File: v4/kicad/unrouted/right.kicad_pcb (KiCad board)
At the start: 2 copper layers, 160 x 118.6 mm, 72 parts

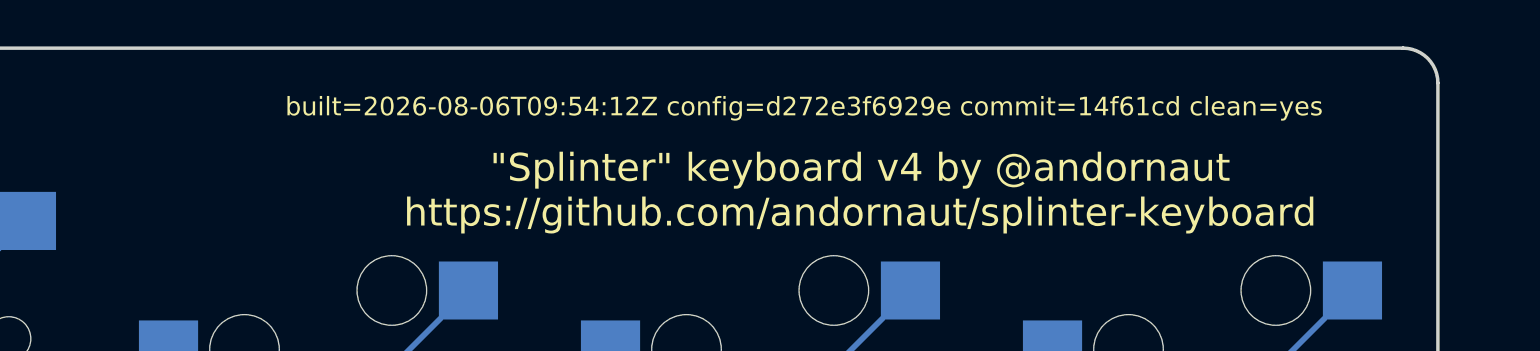
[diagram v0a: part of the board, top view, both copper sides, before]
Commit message: Rebuild the v4 boards from config d272e3f6929e
Pipeline re-run with no config change: new provenance stamp, reordered
items and re-tessellated zone fills. Tracks, vias and footprints are
unchanged on all four boards. KiCad 10 adds td_enabled and empty net
color/assignment maps to each .kicad_pro.
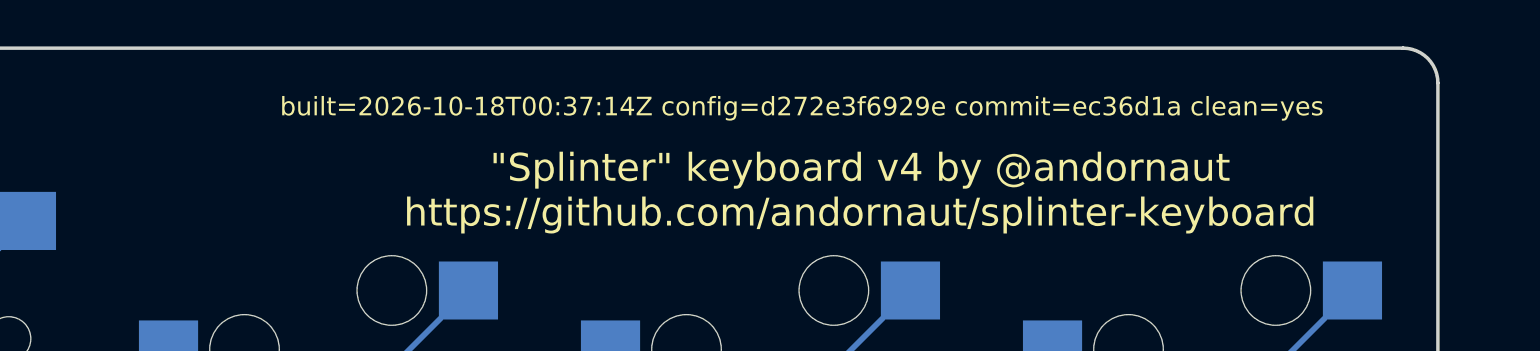
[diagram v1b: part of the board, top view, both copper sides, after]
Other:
- board text added: "built=2026-10-18T00:37:14Z config=d272e3f6929e commit=ec36d1a clean=yes"
- board text removed: "built=2026-08-06T09:54:12Z config=d272e3f6929e commit=14f61cd clean=yes"

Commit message: Wire the v4 TRRS jack per contact and drop the data resistor
- Remove the 100R series resistor from the split data line. QMK's RP2040
  half-duplex driver has the receiving half drive the line high while the
  sender pulls it low, so series resistance lifts the low past the input
  threshold and the link fails.
- Add trrs_hc_pj320a, a single-sided HC-PJ-320A-4P-D footprint with one pad
  per contact at HCTL's recommended positions. Wire tip VCC, ring 2 GP2,
  sleeve GND and leave ring 1 open.
- Re-route the jack and TVS on both halves with the TVS in line.
- Check the jack's contact nets in validate:firmware, and treat the jack as
  non-mirrorable in validate:symmetry.
- Remove the plate wall down to the plate over the TRRS corner, with a 29.00
  relief, so no case surface can touch the jack's exposed contacts. Update
  gen-case.py, BUILD.md and the Onshape exports.
- Document the split connection, the 3.6V Liatris VCC jumper and the
  no-hot-plug rule.
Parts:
- removed R1: 100R, splinter:R_0805
- TRRS1: footprint ceoloide:trrs_pj320a (reversible, symmetric) -> splinter:trrs_hc_pj320a
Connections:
- D33 pad A: DATA_RAW -> P2
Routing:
- net DATA_RAW: track 31.4 -> 0.00 mm
- net P2: track 19.5 -> 37.4 mm
- net GND: track 81.0 -> 71.2 mm
- net P16: track 178.1 -> 169.7 mm
- net P15: track 147.6 -> 139.2 mm
- net P14: track 198.9 -> 190.5 mm
- net P10: track 150.6 -> 142.2 mm
- net P9: track 199.0 -> 194.2 mm
- net dash_upper: track 13.7 -> 12.5 mm, vias 1 -> 0
- net dash_num: track 13.7 -> 12.5 mm, vias 1 -> 0
- net dash_lower: track 13.7 -> 12.5 mm, vias 1 -> 0
- net dash_home: track 13.7 -> 12.5 mm, vias 1 -> 0
- net zero_upper: track 13.7 -> 12.5 mm, vias 1 -> 0
- net zero_num: track 13.7 -> 12.5 mm, vias 1 -> 0
- net zero_lower: track 13.7 -> 12.5 mm, vias 1 -> 0
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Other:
- board text added: "built=2026-10-18T19:11:44Z config=fba23081ee07 commit=0d913c5 clean=no"
- board text removed: "Resistor 100R 1% UNI-ROYAL 0805W8F- 1000T5E 0805"
- board text removed: "built=2026-10-18T00:37:14Z config=d272e3f6929e commit=ec36d1a clean=yes"

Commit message: Rebuild the v4 boards from config fba23081ee07
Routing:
- net P15: track 139.2 -> 147.6 mm
- net P14: track 190.5 -> 198.9 mm
- net P16: track 169.7 -> 178.1 mm
- net P10: track 142.2 -> 150.6 mm
- net P9: track 194.2 -> 199.0 mm
- net dash_upper: track 12.5 -> 13.7 mm, vias 0 -> 1
- net dash_num: track 12.5 -> 13.7 mm, vias 0 -> 1
- net dash_lower: track 12.5 -> 13.7 mm, vias 0 -> 1
- net dash_home: track 12.5 -> 13.7 mm, vias 0 -> 1
- net zero_upper: track 12.5 -> 13.7 mm, vias 0 -> 1
- net zero_num: track 12.5 -> 13.7 mm, vias 0 -> 1
- net zero_lower: track 12.5 -> 13.7 mm, vias 0 -> 1
- net zero_home: track 12.5 -> 13.7 mm, vias 0 -> 1
- net mirror_three_mod: track 13.3 -> 14.5 mm, vias 0 -> 1
- net mirror_four_upper: track 12.5 -> 13.7 mm, vias 0 -> 1
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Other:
- board text added: "built=2026-10-18T19:58:37Z config=fba23081ee07 commit=c602086 clean=yes"
- board text removed: "built=2026-10-18T19:11:44Z config=fba23081ee07 commit=0d913c5 clean=no"

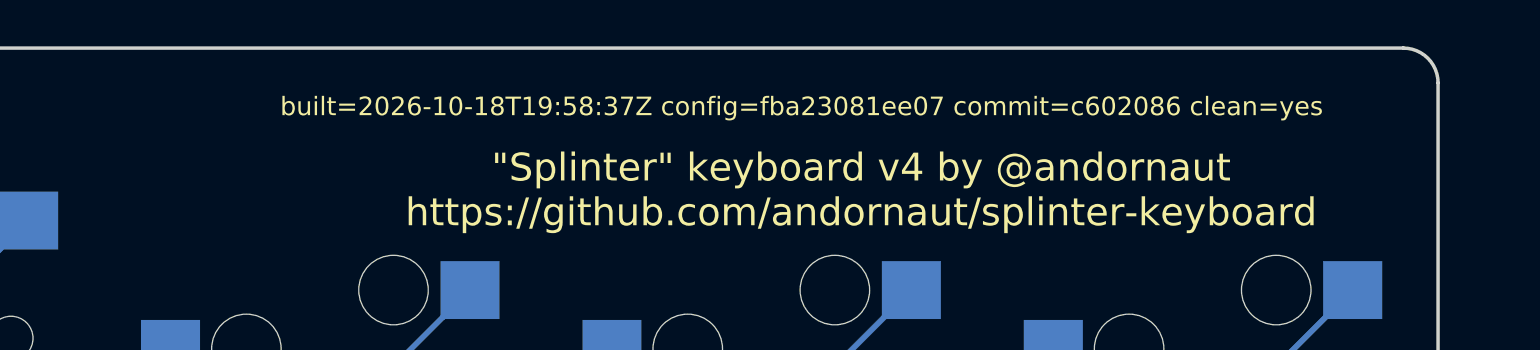
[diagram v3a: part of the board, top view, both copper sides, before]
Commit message: Have JLCPCB place the v4 reset switch
- Add sw_skqgabe010, a fork of ergogen's button footprint whose module layer
  follows `side`, so the position file reports the back-side reset switch on
  the Bottom instead of the bare Top. Pads and silk are unchanged.
- Assign C115351 (ALPS SKQGABE010) in jlcpcb-parts.json at rotation 0: the
  footprint matches JLCPCB's KEY-SMD_4P-L5.2-W5.2-P3.70-LS6.4 at 0 degrees.
- Move the reset switch from hand-soldered to placed by JLCPCB in the v4
  fabrication docs.
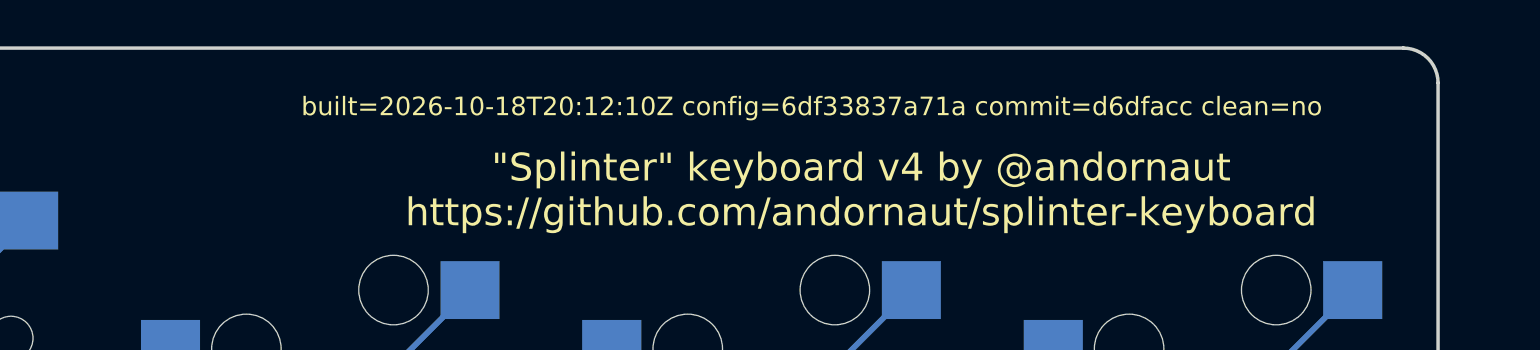
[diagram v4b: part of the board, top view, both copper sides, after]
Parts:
- B1: moved to B.Cu
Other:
- board text added: "built=2026-10-18T20:12:10Z config=6df33837a71a commit=d6dfacc clean=no"
- board text removed: "built=2026-10-18T19:58:37Z config=fba23081ee07 commit=c602086 clean=yes"

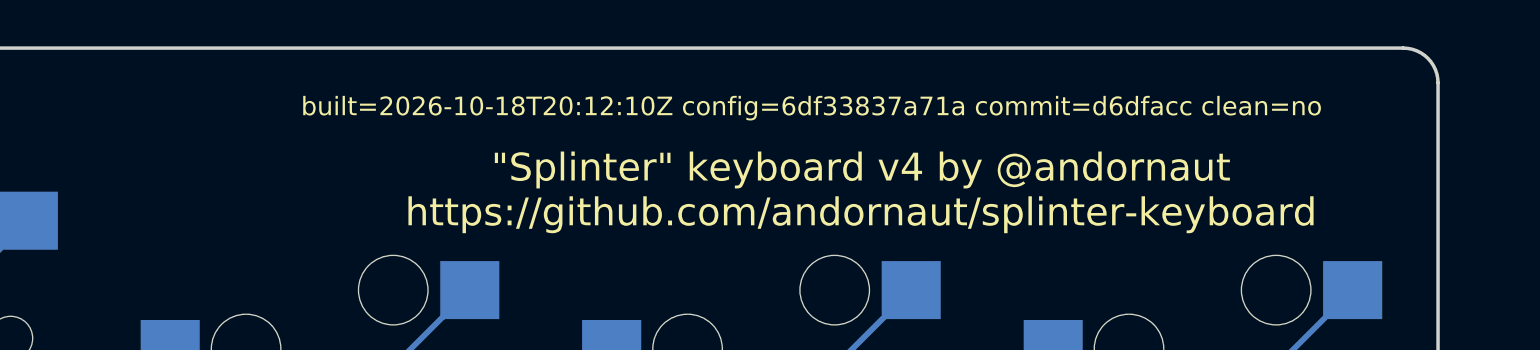
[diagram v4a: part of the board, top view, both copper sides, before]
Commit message: Rebuild the v4 boards from config 6df33837a71a
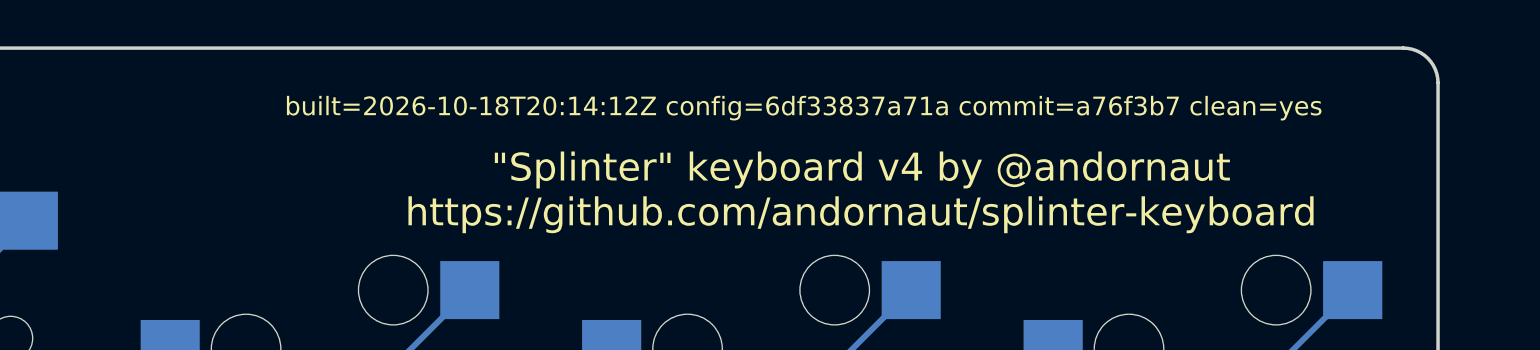
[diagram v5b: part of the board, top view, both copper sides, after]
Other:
- board text added: "built=2026-10-18T20:14:12Z config=6df33837a71a commit=a76f3b7 clean=yes"
- board text removed: "built=2026-10-18T20:12:10Z config=6df33837a71a commit=d6dfacc clean=no"

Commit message: Keep copper out from under the v4 reset switch frame
Add a back-copper rule area between each side's two reset-switch pads, the
prohibited area for copper tracks on ALPS's SKQG land drawing. It disallows
pour, tracks and vias on the switch's own layer only, so the F.Cu matrix
traces under the switch stay. add-keepout-zones.py maps the area from the
footprint frame through the switch's own pads, so it follows the part on both
halves.
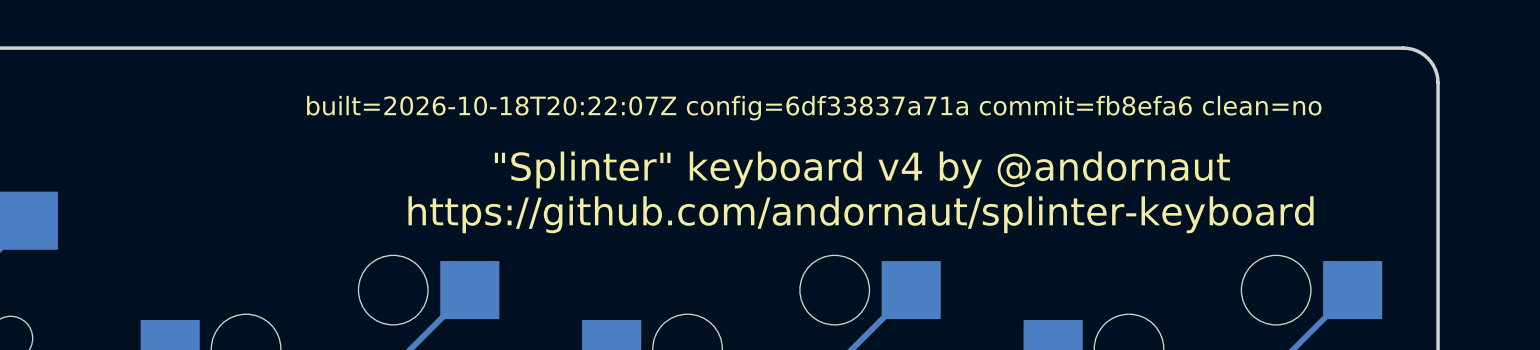
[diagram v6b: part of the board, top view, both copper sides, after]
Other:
- board text added: "built=2026-10-18T20:22:07Z config=6df33837a71a commit=fb8efa6 clean=no"
- board text removed: "built=2026-10-18T20:14:12Z config=6df33837a71a commit=a76f3b7 clean=yes"

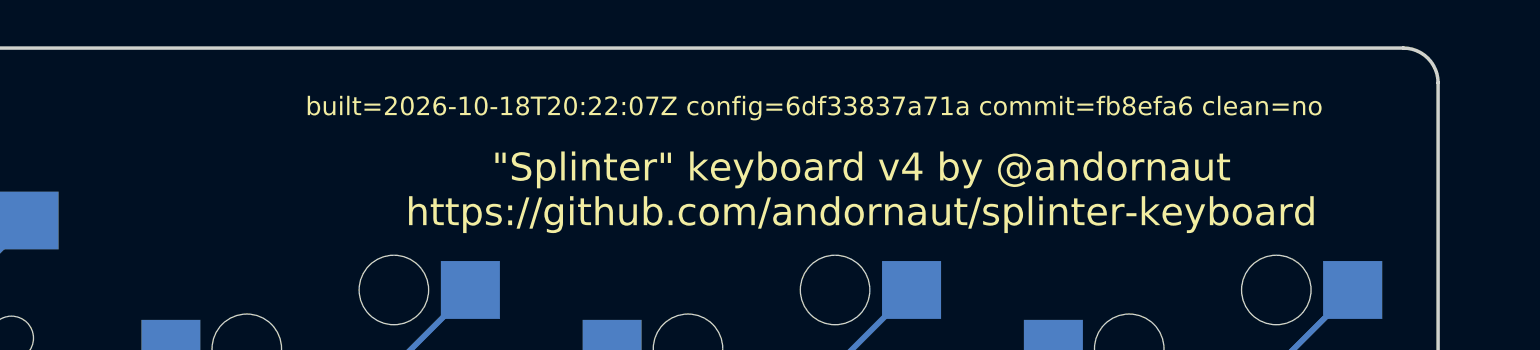
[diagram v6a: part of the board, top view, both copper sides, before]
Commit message: Rebuild the v4 boards from config 6df33837a71a
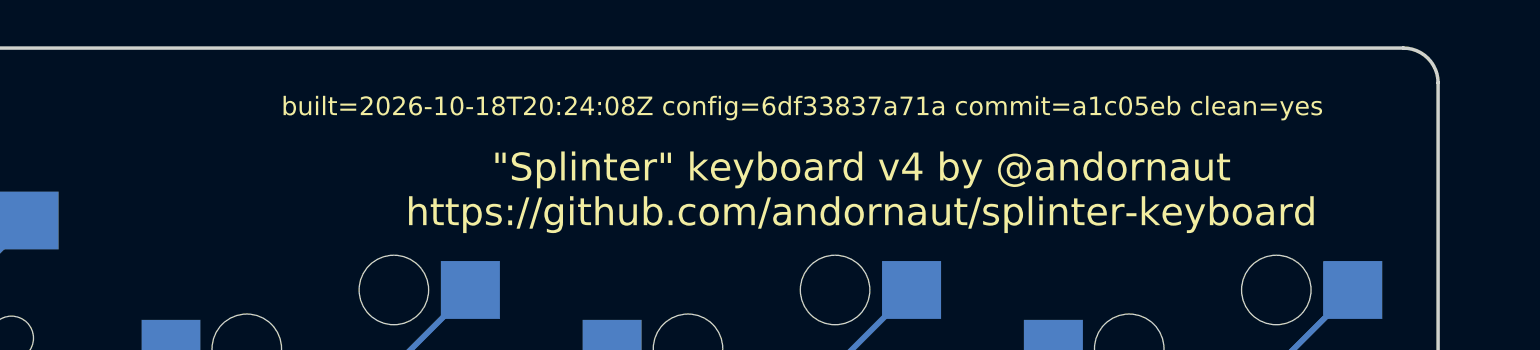
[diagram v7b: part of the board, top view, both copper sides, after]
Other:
- board text added: "built=2026-10-18T20:24:08Z config=6df33837a71a commit=a1c05eb clean=yes"
- board text removed: "built=2026-10-18T20:22:07Z config=6df33837a71a commit=fb8efa6 clean=no"

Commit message: Clear the pour around the v4 reset switch, and correct the order docs
- Add a pour-only rule area around each reset switch and its four pads, so
  the GND pour leaves a clean rectangle there. Tracks stay allowed: the
  switch's own GND and RST traces run along its pad rows.
- JLCCNC: annotate the overall cavity (161.00 x 119.59) and plate
  (160.60 x 119.14) sizes, which are what the parts measure; give the shell
  and plate order remarks; the shell PDFs carry only the thread callouts.
- State the 3.6V jumper hazard for the case where the half with USB is
  still at 5V.
- BUILD.md: the board's pocket play is 0.48-0.50 per side.
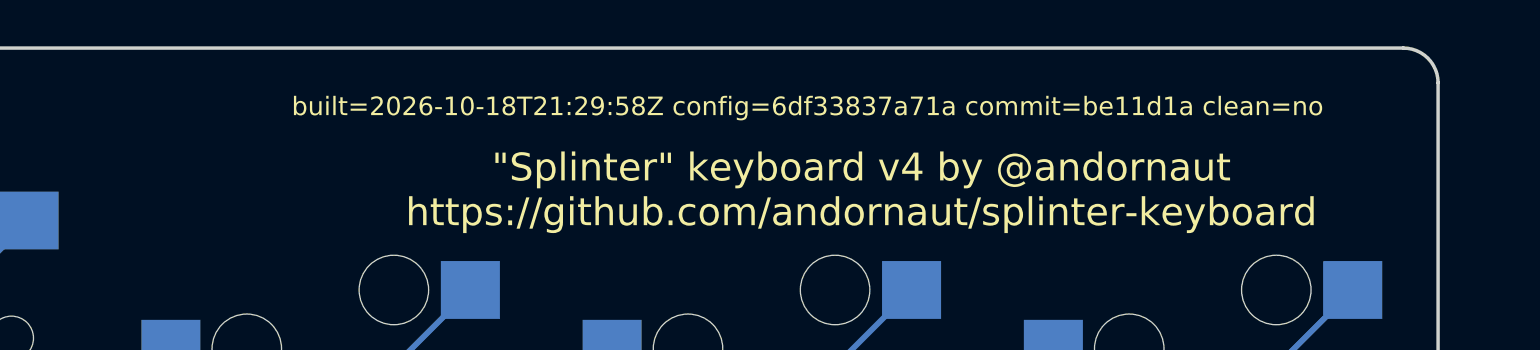
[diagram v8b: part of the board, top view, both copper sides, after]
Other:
- board text added: "built=2026-10-18T21:29:58Z config=6df33837a71a commit=be11d1a clean=no"
- board text removed: "built=2026-10-18T20:24:08Z config=6df33837a71a commit=a1c05eb clean=yes"
